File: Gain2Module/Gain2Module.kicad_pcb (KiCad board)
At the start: 2 copper layers, 56 x 60 mm, 19 parts, among them J1 SigIn, J2 SigOut, J3 Heater, J4 HeaterOut, J5 HV, J6 HVOut, U1 ECC83

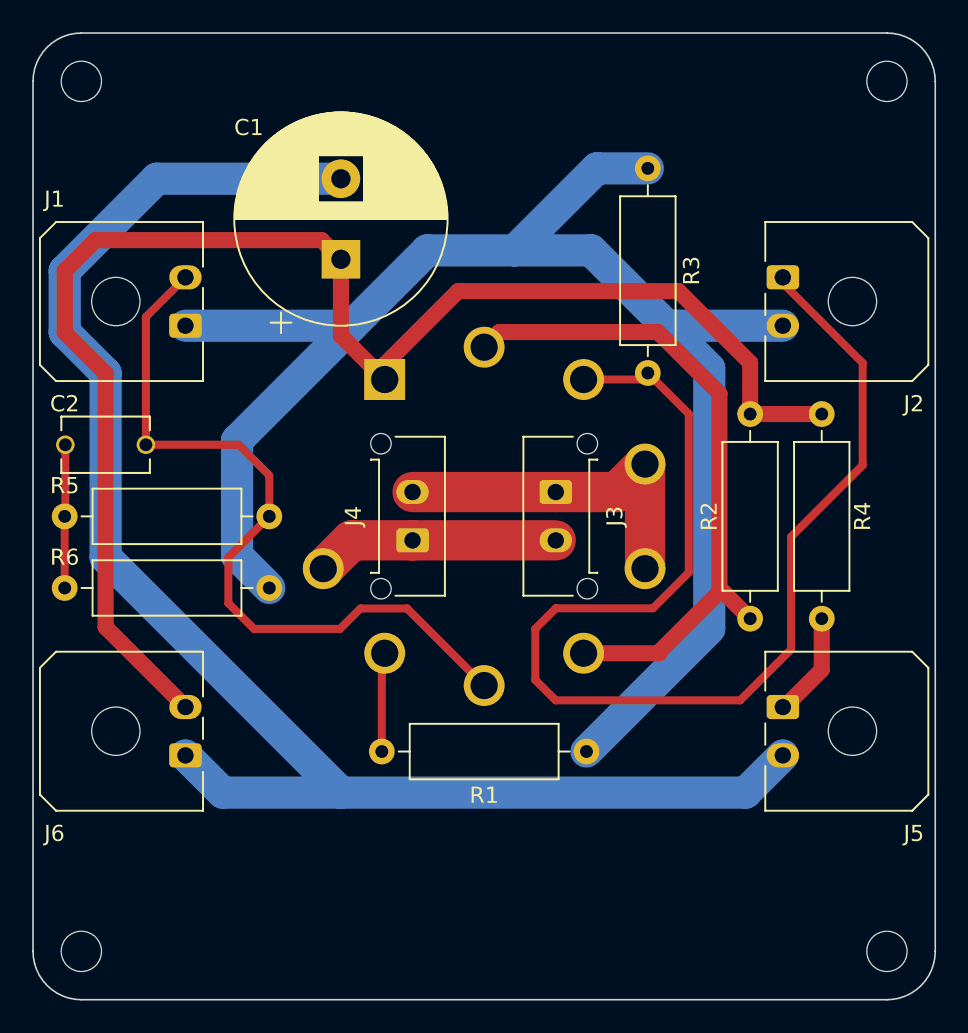
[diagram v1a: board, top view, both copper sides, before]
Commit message: Standardized hole size across all boards
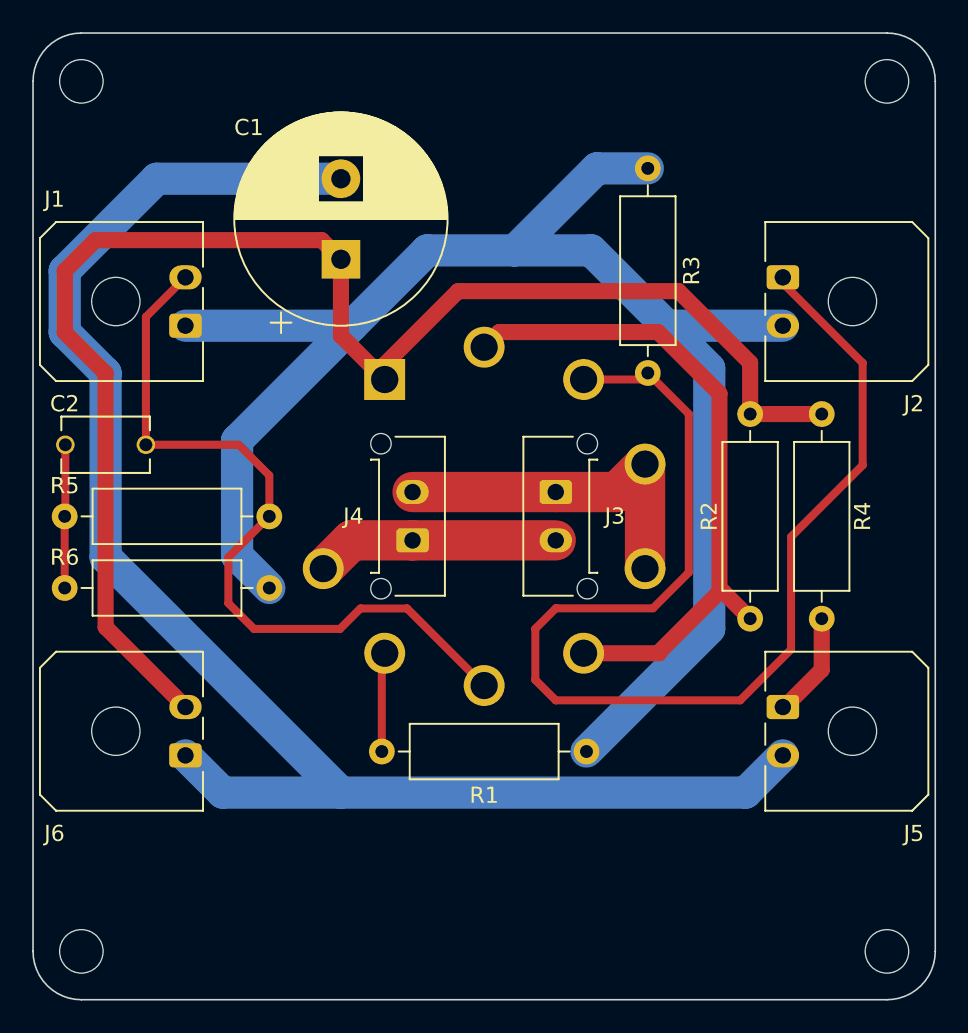
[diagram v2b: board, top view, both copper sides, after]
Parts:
- removed the REF** at (158.3, 69.5)
- removed the REF** at (108.3, 69.5)
- removed the REF** at (158.3, 123.5)
- removed the REF** at (108.3, 123.5)
- added REF**: MountingHole_2.7mm_M2.5, MountingHole:MountingHole_2.7mm_M2.5, F.Cu at (158.3, 69.5)
- added REF**: MountingHole_2.7mm_M2.5, MountingHole:MountingHole_2.7mm_M2.5, F.Cu at (108.3, 123.5)
- added REF**: MountingHole_2.7mm_M2.5, MountingHole:MountingHole_2.7mm_M2.5, F.Cu at (158.3, 123.5)
- added REF**: MountingHole_2.7mm_M2.5, MountingHole:MountingHole_2.7mm_M2.5, F.Cu at (108.3, 69.5)
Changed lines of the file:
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@@
     )
   )
-  (footprint "MountingHole:MountingHole_2.5mm" (layer "F.Cu")
+  (footprint "MountingHole:MountingHole_2.7mm_M2.5" (layer "F.Cu")
     (at 158.35 69.53)
-    (descr "Mounting Hole 2.5mm, no annular")
-    (tags "mounting hole 2.5mm no annular")
+    (descr "Mounting Hole 2.7mm, no annular, M2.5")
+    (tags "mounting hole 2.7mm no annular m2.5")
     (attr exclude_from_pos_files exclude_from_bom)
-    (fp_text reference "REF**" (at 0 -3.5) (layer "F.SilkS") hide
-        (effects (font (size 1 1) (thickness 0.15)))
-    )
-    (fp_text value "MountingHole_2.5mm" (at 0 3.5) (layer "F.Fab") hide
+    (fp_text reference "REF**" (at 0 -3.7) (layer "F.SilkS") hide
+        (effects (font (size 1 1) (thickness 0.15)))
+    )
+    (fp_text value "MountingHole_2.7mm_M2.5" (at 0 3.7) (layer "F.Fab") hide
         (effects (font (size 1 1) (thickness 0.15)))
     )
@@
         (effects (font (size 1 1) (thickness 0.15)))
     )
-    (fp_circle (center 0 0) (end 2.5 0)
+    (fp_circle (center 0 0) (end 2.7 0)
       (stroke (width 0.15) (type solid)) (fill none) (layer "Cmts.User"))
-    (fp_circle (center 0 0) (end 2.75 0)
+    (fp_circle (center 0 0) (end 2.95 0)
       (stroke (width 0.05) (type solid)) (fill none) (layer "F.CrtYd"))
-    (pad "" np_thru_hole circle (at 0 0) (size 2.5 2.5) (drill 2.5) (layers "F&B.Cu" "*.Mask"))
+    (pad "" np_thru_hole circle (at 0 0) (size 2.7 2.7) (drill 2.7) (layers "*.Cu" "*.Mask"))
   )
   (footprint "Capacitor_THT:CP_Radial_D13.0mm_P5.00mm" (layer "F.Cu")
@@
     (property "ki_keywords" "screw terminal")
     (attr through_hole)
-    (fp_text reference "J4" (at 1.5 -3.67 90) (layer "F.SilkS")
+    (fp_text reference "J4" (at 1.5 -3.67 180) (layer "F.SilkS")
         (effects (font (size 1 1) (thickness 0.15)))
     )
@@
       (rotate (xyz 90 0 180))
     )
+  )
+  (footprint "MountingHole:MountingHole_2.7mm_M2.5" (layer "F.Cu")
+    (at 108.35 123.53)
+    (descr "Mounting Hole 2.7mm, no annular, M2.5")
+    (tags "mounting hole 2.7mm no annular m2.5")
+    (attr exclude_from_pos_files exclude_from_bom)
+    (fp_text reference "REF**" (at 0 -3.7) (layer "F.SilkS") hide
+        (effects (font (size 1 1) (thickness 0.15)))
+    )
+    (fp_text value "MountingHole_2.7mm_M2.5" (at 0 3.7) (layer "F.Fab") hide
+        (effects (font (size 1 1) (thickness 0.15)))
+    )
+    (fp_text user "${REFERENCE}" (at 0 0) (layer "F.Fab")
+        (effects (font (size 1 1) (thickness 0.15)))
+    )
+    (fp_circle (center 0 0) (end 2.7 0)
+      (stroke (width 0.15) (type solid)) (fill none) (layer "Cmts.User"))
+    (fp_circle (center 0 0) (end 2.95 0)
+      (stroke (width 0.05) (type solid)) (fill none) (layer "F.CrtYd"))
+    (pad "" np_thru_hole circle (at 0 0) (size 2.7 2.7) (drill 2.7) (layers "*.Cu" "*.Mask"))
   )
   (footprint "Resistor_THT:R_Axial_DIN0309_L9.0mm_D3.2mm_P12.70mm_Horizontal" (layer "F.Cu")
@@
     )
   )
-  (footprint "MountingHole:MountingHole_2.5mm" (layer "F.Cu")
-    (at 108.35 69.53)
-    (descr "Mounting Hole 2.5mm, no annular")
-    (tags "mounting hole 2.5mm no annular")
+  (footprint "MountingHole:MountingHole_2.7mm_M2.5" (layer "F.Cu")
+    (at 158.35 123.53)
+    (descr "Mounting Hole 2.7mm, no annular, M2.5")
+    (tags "mounting hole 2.7mm no annular m2.5")
     (attr exclude_from_pos_files exclude_from_bom)
-    (fp_text reference "REF**" (at 0 -3.5) (layer "F.SilkS") hide
-        (effects (font (size 1 1) (thickness 0.15)))
-    )
-    (fp_text value "MountingHole_2.5mm" (at 0 3.5) (layer "F.Fab") hide
+    (fp_text reference "REF**" (at 0 -3.7) (layer "F.SilkS") hide
+        (effects (font (size 1 1) (thickness 0.15)))
+    )
+    (fp_text value "MountingHole_2.7mm_M2.5" (at 0 3.7) (layer "F.Fab") hide
         (effects (font (size 1 1) (thickness 0.15)))
     )
@@
         (effects (font (size 1 1) (thickness 0.15)))
     )
-    (fp_circle (center 0 0) (end 2.5 0)
+    (fp_circle (center 0 0) (end 2.7 0)
       (stroke (width 0.15) (type solid)) (fill none) (layer "Cmts.User"))
-    (fp_circle (center 0 0) (end 2.75 0)
+    (fp_circle (center 0 0) (end 2.95 0)
       (stroke (width 0.05) (type solid)) (fill none) (layer "F.CrtYd"))
-    (pad "" np_thru_hole circle (at 0 0) (size 2.5 2.5) (drill 2.5) (layers "F&B.Cu" "*.Mask"))
+    (pad "" np_thru_hole circle (at 0 0) (size 2.7 2.7) (drill 2.7) (layers "*.Cu" "*.Mask"))
   )
   (footprint "CustomFootprints:Molex_Micro-Fit_3.0_43650-0200_1x02_P3.00mm_Horizontal" (layer "F.Cu")
@@
       (rotate (xyz 0 0 180))
     )
-  )
-  (footprint "MountingHole:MountingHole_2.5mm" (layer "F.Cu")
-    (at 158.35 123.53)
-    (descr "Mounting Hole 2.5mm, no annular")
-    (tags "mounting hole 2.5mm no annular")
-    (attr exclude_from_pos_files exclude_from_bom)
-    (fp_text reference "REF**" (at 0 -3.5) (layer "F.SilkS") hide
-        (effects (font (size 1 1) (thickness 0.15)))
-    )
-    (fp_text value "MountingHole_2.5mm" (at 0 3.5) (layer "F.Fab") hide
-        (effects (font (size 1 1) (thickness 0.15)))
-    )
-    (fp_text user "${REFERENCE}" (at 0 0) (layer "F.Fab")
-        (effects (font (size 1 1) (thickness 0.15)))
-    )
-    (fp_circle (center 0 0) (end 2.5 0)
-      (stroke (width 0.15) (type solid)) (fill none) (layer "Cmts.User"))
-    (fp_circle (center 0 0) (end 2.75 0)
-      (stroke (width 0.05) (type solid)) (fill none) (layer "F.CrtYd"))
-    (pad "" np_thru_hole circle (at 0 0) (size 2.5 2.5) (drill 2.5) (layers "F&B.Cu" "*.Mask"))
-  )
-  (footprint "MountingHole:MountingHole_2.5mm" (layer "F.Cu")
-    (at 108.35 123.53)
-    (descr "Mounting Hole 2.5mm, no annular")
-    (tags "mounting hole 2.5mm no annular")
-    (attr exclude_from_pos_files exclude_from_bom)
-    (fp_text reference "REF**" (at 0 -3.5) (layer "F.SilkS") hide
-        (effects (font (size 1 1) (thickness 0.15)))
-    )
-    (fp_text value "MountingHole_2.5mm" (at 0 3.5) (layer "F.Fab") hide
-        (effects (font (size 1 1) (thickness 0.15)))
-    )
-    (fp_text user "${REFERENCE}" (at 0 0) (layer "F.Fab")
-        (effects (font (size 1 1) (thickness 0.15)))
-    )
-    (fp_circle (center 0 0) (end 2.5 0)
-      (stroke (width 0.15) (type solid)) (fill none) (layer "Cmts.User"))
-    (fp_circle (center 0 0) (end 2.75 0)
-      (stroke (width 0.05) (type solid)) (fill none) (layer "F.CrtYd"))
-    (pad "" np_thru_hole circle (at 0 0) (size 2.5 2.5) (drill 2.5) (layers "F&B.Cu" "*.Mask"))
   )
   (footprint "CustomFootprints:Molex_Micro-Fit_3.0_43650-0200_1x02_P3.00mm_Horizontal" (layer "F.Cu")
@@
     (property "ki_keywords" "screw terminal")
     (attr through_hole)
-    (fp_text reference "J3" (at 1.5 -3.67 -90) (layer "F.SilkS")
+    (fp_text reference "J3" (at 1.5 -3.67) (layer "F.SilkS")
         (effects (font (size 1 1) (thickness 0.15)))
     )
@@
     )
   )
+  (footprint "MountingHole:MountingHole_2.7mm_M2.5" (layer "F.Cu")
+    (at 108.35 69.53)
+    (descr "Mounting Hole 2.7mm, no annular, M2.5")
+    (tags "mounting hole 2.7mm no annular m2.5")
+    (attr exclude_from_pos_files exclude_from_bom)
+    (fp_text reference "REF**" (at 0 -3.7) (layer "F.SilkS") hide
+        (effects (font (size 1 1) (thickness 0.15)))
+    )
+    (fp_text value "MountingHole_2.7mm_M2.5" (at 0 3.7) (layer "F.Fab") hide
+        (effects (font (size 1 1) (thickness 0.15)))
+    )
+    (fp_text user "${REFERENCE}" (at 0 0) (layer "F.Fab")
+        (effects (font (size 1 1) (thickness 0.15)))
+    )
+    (fp_circle (center 0 0) (end 2.7 0)
+      (stroke (width 0.15) (type solid)) (fill none) (layer "Cmts.User"))
+    (fp_circle (center 0 0) (end 2.95 0)
+      (stroke (width 0.05) (type solid)) (fill none) (layer "F.CrtYd"))
+    (pad "" np_thru_hole circle (at 0 0) (size 2.7 2.7) (drill 2.7) (layers "*.Cu" "*.Mask"))
+  )
   (footprint "Resistor_THT:R_Axial_DIN0309_L9.0mm_D3.2mm_P12.70mm_Horizontal" (layer "F.Cu")
